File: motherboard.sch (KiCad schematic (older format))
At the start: 90 parts, among them P1 CONN_02X08, U1 STM32F411-LQFP64, U10 74LS125, U11 74LS125, U12 74LS125, U13 74LS125, U14 PCA9517A, U15 PCA9517A, U16 74LS125, U17 74LS125, U2 STM32F411-LQFP64, U3 AP7313, U4 74LS00, U5 74LS125, U6 FM25V20A-G, U7 FM25V20A-G, U8 FM25V20A-G, U9 FM25V20A-G, Y1 32k, Y2 8M(16pF), Y3 32k, Y4 8M(16pF)

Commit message: Implemented recommendations from design meeting.
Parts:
- added C27, C28: 1uF, symbol C
- added C29, C30, C31, C32, C33: 0.1uF, symbol C
- added R18, R25, R26, R27, R28, R29: 100K, symbol R
- added unit 3 of U4
- added unit 4 of U4
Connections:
- net +3V3: now also C29.1, C31.1, C32.1, R18.2, R25.2, R26.2, R27.2, U4.14 (VCC), U4.14 (VCC)
- net GND: now also C27.1, C28.1, C29.2, C30.2, C31.2, C32.2, C33.2, R28.1, R29.1, U4.7 (GND), U4.7 (GND)
- net GPIO0: now also H1.51 (P51); no longer H1.1 (P1)
- net GPIO1: now also H1.52 (P52); no longer H1.2 (P2)
- net GPIO10: now also H1.39 (P39); no longer H1.13 (P13)
- net GPIO11: now also H1.40 (P40); no longer H1.14 (P14)
- net GPIO12: now also H1.37 (P37); no longer H1.15 (P15)
- net GPIO13: now also U2.2 (PC13); no longer H1.16 (P16), U1.54 (PD2)
- net GPIO2: now also H1.49 (P49); no longer H1.3 (P3)
- net GPIO3: now also H1.50 (P50); no longer H1.4 (P4)
- net GPIO4: now also H1.45 (P45); no longer H1.7 (P7)
- net GPIO5: now also H1.46 (P46); no longer H1.8 (P8)
- net GPIO6: now also H1.43 (P43); no longer H1.9 (P9)
- net GPIO7: now also H1.44 (P44); no longer H1.10 (P10)
- net GPIO8: now also H1.41 (P41); no longer H1.11 (P11)
- net GPIO9: now also H1.42 (P42); no longer H1.12 (P12)
- net I2C2_SCL: now also H1.1 (P1), H1.34 (P34); no longer H1.20 (P20), H1.51 (P51)
- net I2C2_SDA: now also H1.3 (P3), H1.33 (P33); no longer H1.19 (P19), H1.49 (P49)
- net NBUFEN_PRI: now also H1.5 (P5), C30.1; no longer H1.47 (P47)
- net NBUFEN_SEC: now also H1.6 (P6), C33.1; no longer H1.48 (P48)
- net NRST_P: now also C27.2, U4.8; no longer U2.50 (PA15)
- net NRST_S: now also C28.2, U4.11; no longer U1.50 (PA15)
- net RADIO_RR: now also H1.48 (P48); no longer H1.6 (P6)
- net RADIO_RX: now also H1.35 (P35); no longer H1.17 (P17)
- net RADIO_TR: now also H1.47 (P47); no longer H1.5 (P5)
- net RADIO_TX: now also H1.36 (P36), R29.2; no longer H1.18 (P18)
- net SGPIO10: now also H1.18 (P18); no longer H1.36 (P36)
- net SGPIO11: now also H1.15 (P15); no longer H1.37 (P37)
- net SGPIO12: now also H1.16 (P16); no longer H1.38 (P38)
- net SGPIO13: now also H1.13 (P13); no longer H1.39 (P39), U2.2 (PC13)
- net SGPIO5: now also H1.4 (P4); no longer H1.50 (P50)
- net SGPIO6: now also H1.2 (P2); no longer H1.52 (P52)
- net SGPIO7: now also H1.19 (P19); no longer H1.33 (P33)
- net SGPIO8: now also H1.20 (P20); no longer H1.34 (P34)
- net SGPIO9: now also H1.17 (P17); no longer H1.35 (P35)
- net SYS_RESET: now also H1.23 (P23), R28.2; no longer H1.29 (P29)
- net SYS_SCL: now also H1.9 (P9); no longer H1.43 (P43)
- net SYS_SDA: now also H1.11 (P11); no longer H1.41 (P41)
- net SYS_SPI_MISO: now also H1.32 (P32); no longer H1.22 (P22)
- net SYS_SPI_MOSI: now also H1.29 (P29); no longer H1.23 (P23)
- net SYS_SPI_NSS: now also H1.30 (P30); no longer H1.24 (P24)
- net SYS_SPI_SCK: now also H1.31 (P31); no longer H1.21 (P21)
- net SGPIO14 renamed NRST2_P
- net NRST2_P: now also R25.1, U4.10; no longer H1.40 (P40)
- new net NRST1_P: R18.1, U2.50 (PA15), U4.9
- new net NRST1_S: R26.1, U1.50 (PA15), U4.12
- new net NRST2_S: R27.1, U1.54 (PD2), U4.13
- no-connect marks 38 -> 40
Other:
- note added: "Not Populated - Tie Down if Unused"
- moved on the sheet: R1, R2, R3, R4, R5, R6, R7, R8, R9, TP1, TP2, TP3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

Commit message: Began placing new components
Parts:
- C27, C28, C29, C30, C31, C32, C33: footprint (none) -> Capacitors_SMD:C_0805_HandSoldering
- R18, R25, R26, R27, R28, R29: footprint (none) -> Resistors_SMD:R_0805_HandSoldering

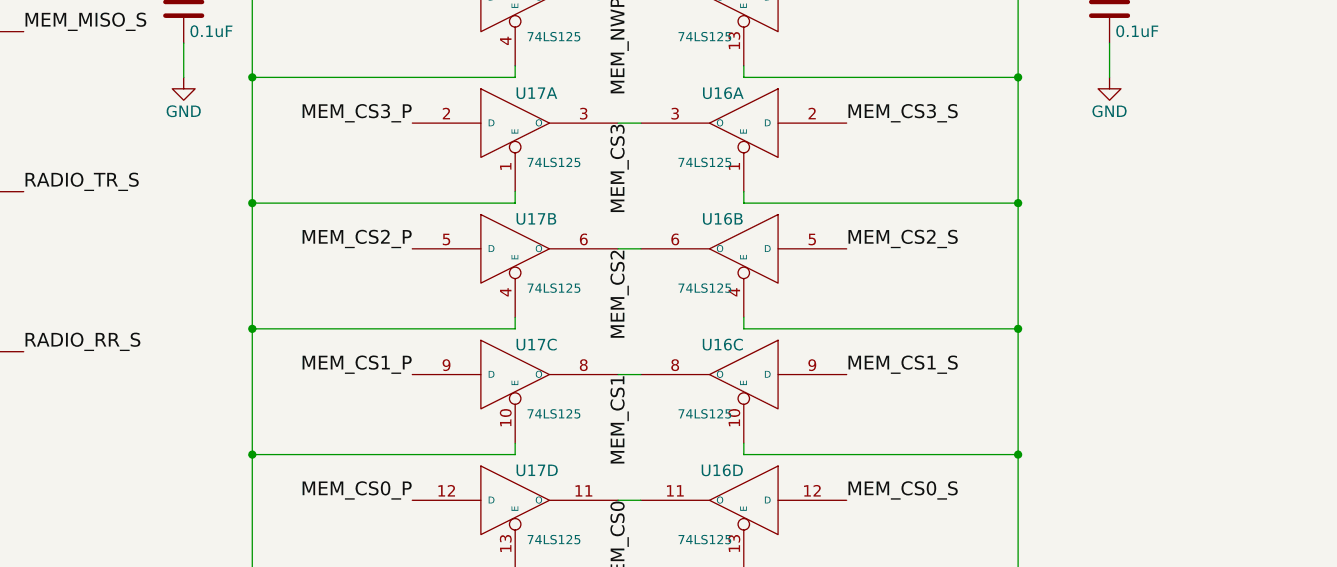
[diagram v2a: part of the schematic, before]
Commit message: All components placed
Most signals routed
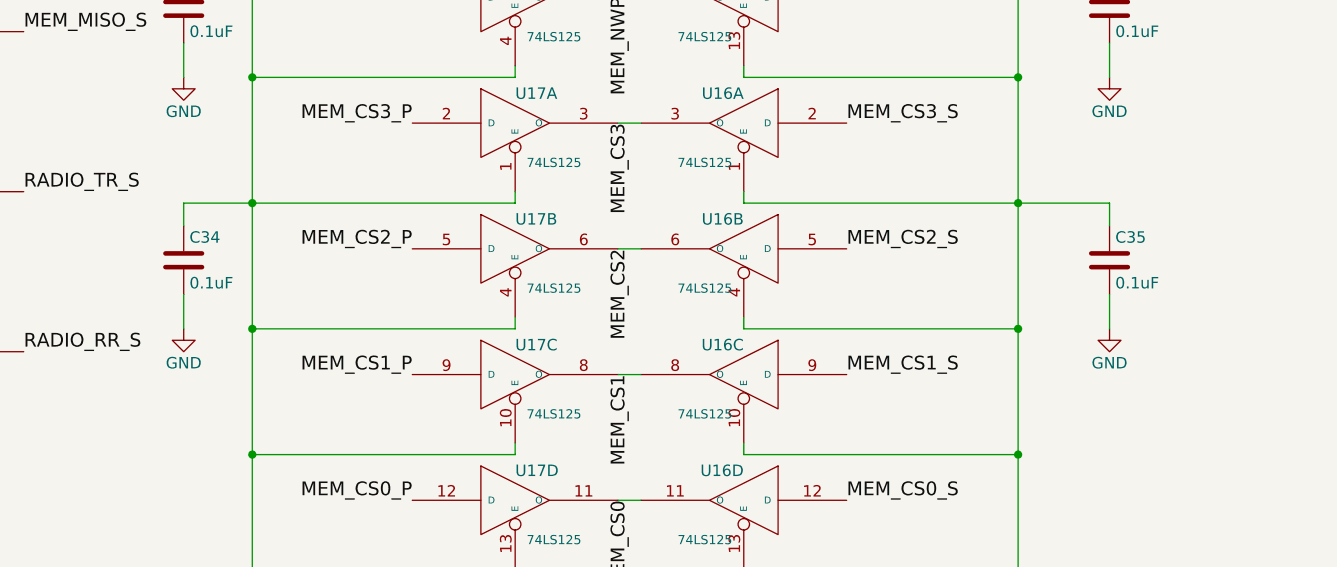
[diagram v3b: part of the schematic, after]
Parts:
- added C34, C35: 0.1uF, Capacitors_SMD:C_0805_HandSoldering, symbol C
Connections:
- net GND: now also C34.2, C35.2
- net NBUFEN_PRI: now also C34.1
- net NBUFEN_SEC: now also C35.1
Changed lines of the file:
@@
 	8350 1950 8350 2150
 Wire Wire Line
-	14150 2400 12950 2400
+	12950 2400 14550 2400
 Wire Wire Line
 	12950 2400 12950 2350
@@
 	11950 2950 11950 2900
 Wire Wire Line
-	11950 2350 11950 2400
+	11950 2400 11950 2350
 Wire Wire Line
 	12400 3150 12500 3150
@@
 Connection ~ 10800 3500
 Wire Wire Line
-	11950 2400 10800 2400
+	10500 2400 11950 2400
 Connection ~ 10800 2950
 Wire Wire Line
@@
 Text Notes 13950 8650 0    60   ~ 0
 Not Populated - Tie Down if Unused
+$Comp
+L GND #PWR062
+U 1 1 5900142E
+P 10500 2950
+F 0 "#PWR062" H 10500 2700 50  0001 C CNN
+F 1 "GND" H 10500 2800 50  0000 C CNN
+F 2 "" H 10500 2950 50  0000 C CNN
+F 3 "" H 10500 2950 50  0000 C CNN
+	1    10500 2950
+	1    0    0    -1
+$EndComp
+$Comp
+L C C34
+U 1 1 59001434
+P 10500 2650
+F 0 "C34" H 10525 2750 50  0000 L CNN
+F 1 "0.1uF" H 10525 2550 50  0000 L CNN
+F 2 "Capacitors_SMD:C_0805_HandSoldering" H 10538 2500 50  0001 C CNN
+F 3 "" H 10500 2650 50  0000 C CNN
+	1    10500 2650
+	1    0    0    -1
+$EndComp
+Wire Wire Line
+	10500 2950 10500 2800
+Wire Wire Line
+	10500 2400 10500 2500
+$Comp
+L GND #PWR063
+U 1 1 5900389F
+P 14550 2950
+F 0 "#PWR063" H 14550 2700 50  0001 C CNN
+F 1 "GND" H 14550 2800 50  0000 C CNN
+F 2 "" H 14550 2950 50  0000 C CNN
+F 3 "" H 14550 2950 50  0000 C CNN
+	1    14550 2950
+	1    0    0    -1
+$EndComp
+$Comp
+L C C35
+U 1 1 590038A5
+P 14550 2650
+F 0 "C35" H 14575 2750 50  0000 L CNN
+F 1 "0.1uF" H 14575 2550 50  0000 L CNN
+F 2 "Capacitors_SMD:C_0805_HandSoldering" H 14588 2500 50  0001 C CNN
+F 3 "" H 14550 2650 50  0000 C CNN
+	1    14550 2650
+	1    0    0    -1
+$EndComp
+Wire Wire Line
+	14550 2950 14550 2800
+Wire Wire Line
+	14550 2400 14550 2500
 $EndSCHEMATC

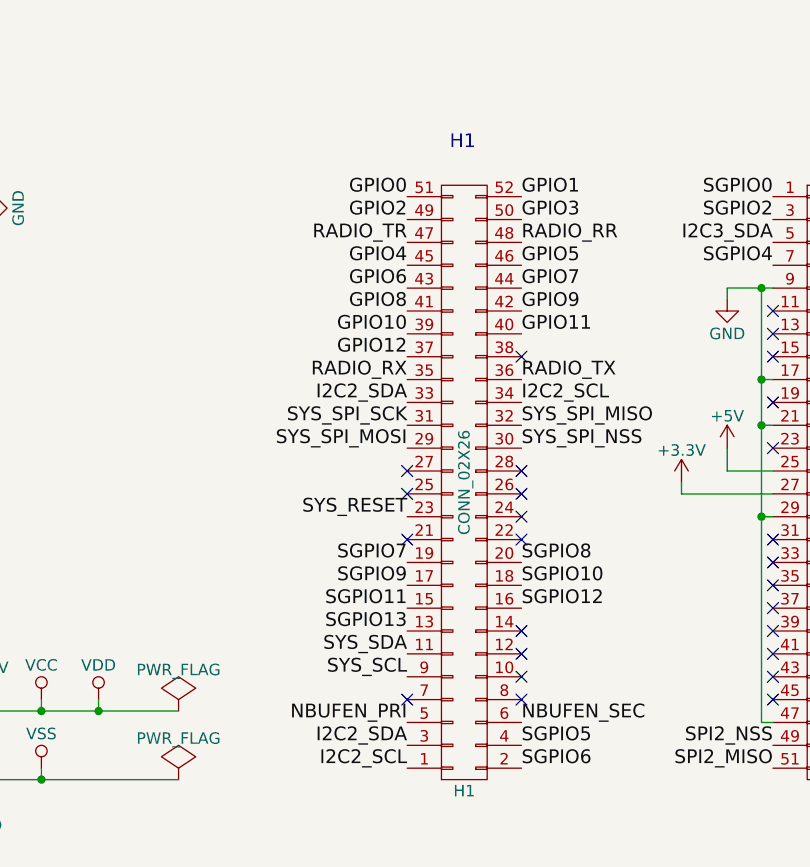
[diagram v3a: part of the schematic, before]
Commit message: Replaced backwards CSK headers
Connectors were mirrored, so that sucks. Connectors replaced,
but all traces to headers need to be re-routed.
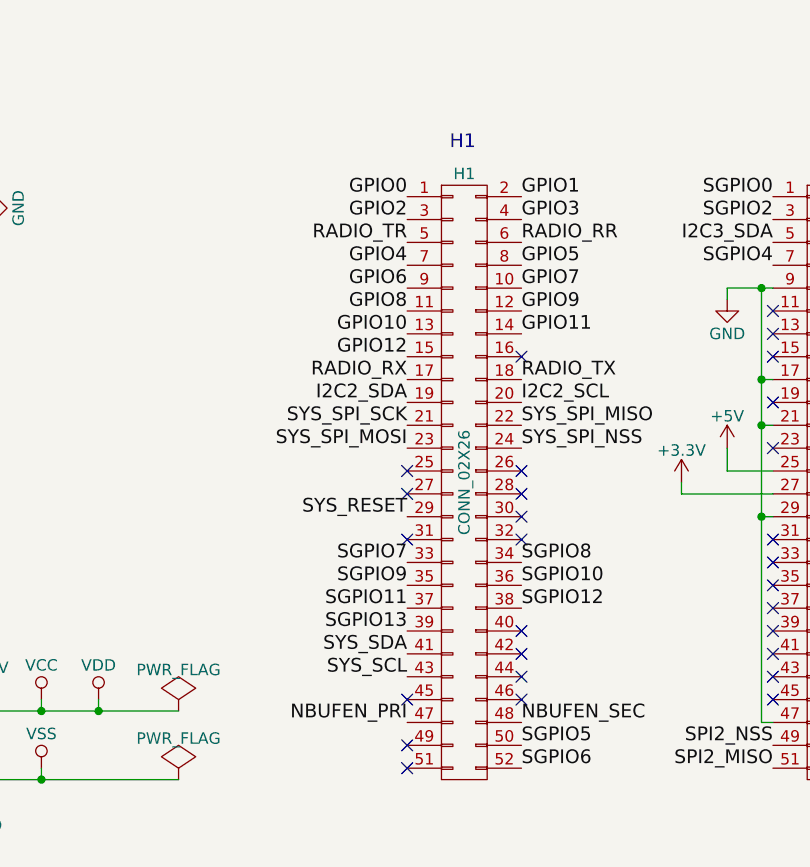
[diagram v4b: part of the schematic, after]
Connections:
- net GPIO0: now also H1.1 (P1); no longer H1.51 (P51)
- net GPIO1: now also H1.2 (P2); no longer H1.52 (P52)
- net GPIO10: now also H1.13 (P13); no longer H1.39 (P39)
- net GPIO11: now also H1.14 (P14); no longer H1.40 (P40)
- net GPIO12: now also H1.15 (P15); no longer H1.37 (P37)
- net GPIO2: now also H1.3 (P3); no longer H1.49 (P49)
- net GPIO3: now also H1.4 (P4); no longer H1.50 (P50)
- net GPIO4: now also H1.7 (P7); no longer H1.45 (P45)
- net GPIO5: now also H1.8 (P8); no longer H1.46 (P46)
- net GPIO6: now also H1.9 (P9); no longer H1.43 (P43)
- net GPIO7: now also H1.10 (P10); no longer H1.44 (P44)
- net GPIO8: now also H1.11 (P11); no longer H1.41 (P41)
- net GPIO9: now also H1.12 (P12); no longer H1.42 (P42)
- net I2C2_SCL: now also H1.20 (P20); no longer H1.1 (P1), H1.34 (P34)
- net I2C2_SDA: now also H1.19 (P19); no longer H1.3 (P3), H1.33 (P33)
- net NBUFEN_PRI: now also H1.47 (P47); no longer H1.5 (P5)
- net NBUFEN_SEC: now also H1.48 (P48); no longer H1.6 (P6)
- net RADIO_RR: now also H1.6 (P6); no longer H1.48 (P48)
- net RADIO_RX: now also H1.17 (P17); no longer H1.35 (P35)
- net RADIO_TR: now also H1.5 (P5); no longer H1.47 (P47)
- net RADIO_TX: now also H1.18 (P18); no longer H1.36 (P36)
- net SGPIO10: now also H1.36 (P36); no longer H1.18 (P18)
- net SGPIO11: now also H1.37 (P37); no longer H1.15 (P15)
- net SGPIO12: now also H1.38 (P38); no longer H1.16 (P16)
- net SGPIO13: now also H1.39 (P39); no longer H1.13 (P13)
- net SGPIO5: now also H1.50 (P50); no longer H1.4 (P4)
- net SGPIO6: now also H1.52 (P52); no longer H1.2 (P2)
- net SGPIO7: now also H1.33 (P33); no longer H1.19 (P19)
- net SGPIO8: now also H1.34 (P34); no longer H1.20 (P20)
- net SGPIO9: now also H1.35 (P35); no longer H1.17 (P17)
- net SYS_RESET: now also H1.29 (P29); no longer H1.23 (P23)
- net SYS_SCL: now also H1.43 (P43); no longer H1.9 (P9)
- net SYS_SDA: now also H1.41 (P41); no longer H1.11 (P11)
- net SYS_SPI_MISO: now also H1.22 (P22); no longer H1.32 (P32)
- net SYS_SPI_MOSI: now also H1.23 (P23); no longer H1.29 (P29)
- net SYS_SPI_NSS: now also H1.24 (P24); no longer H1.30 (P30)
- net SYS_SPI_SCK: now also H1.21 (P21); no longer H1.31 (P31)
- no-connect marks 40 -> 42
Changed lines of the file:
@@
 F 3 "" H 9150 8900 50  0000 C CNN
 	1    9150 9600
-	1    0    0    1
+	1    0    0    -1
 $EndComp
 Text Notes 10800 8150 2    60   ~ 0
@@
 Text Label 8900 10650 2    60   ~ 0
 NBUFEN_PRI
-Text Label 8900 10750 2    60   ~ 0
-I2C2_SDA
-Text Label 8900 10850 2    60   ~ 0
-I2C2_SCL
 Text Label 9400 10850 0    60   ~ 0
 SGPIO6
@@
 Wire Wire Line
 	14550 2400 14550 2500
+NoConn ~ 8900 10750
+NoConn ~ 8900 10850
 $EndSCHEMATC

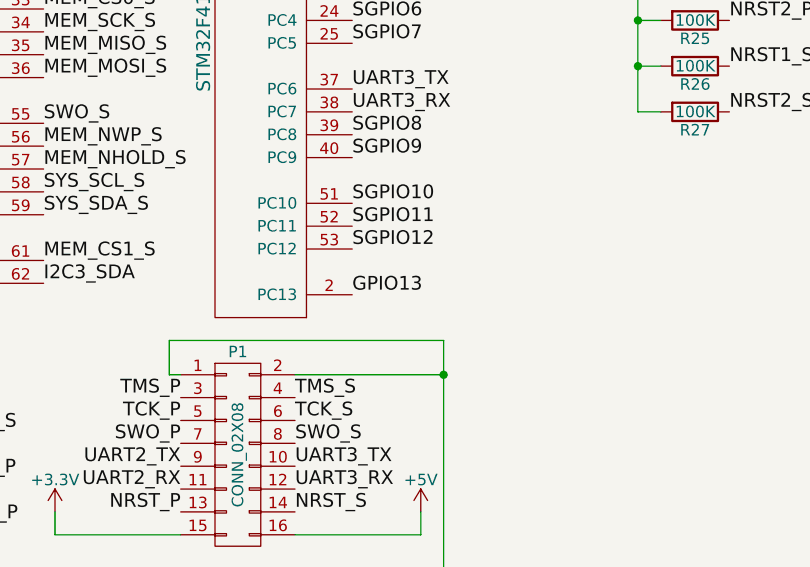
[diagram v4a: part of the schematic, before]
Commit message: Primary GPIO routed
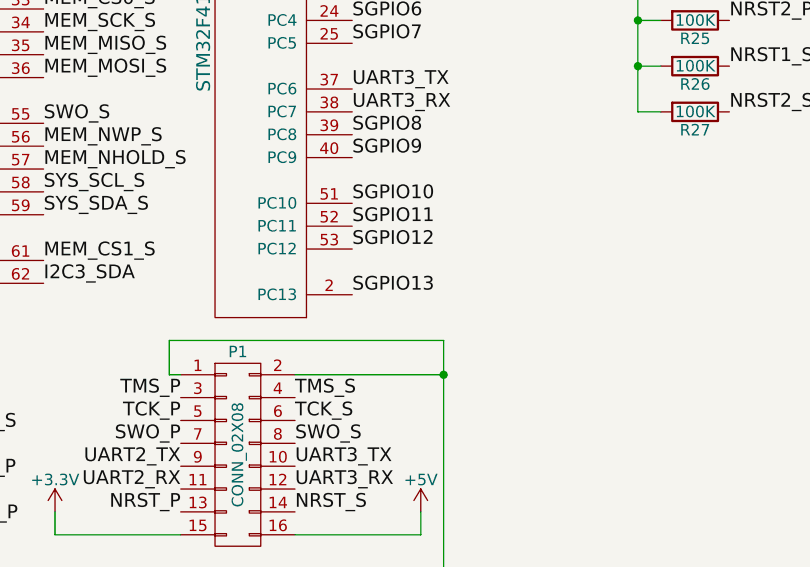
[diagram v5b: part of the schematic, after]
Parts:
- H1, H2: footprint Socket_Strips:Socket_Strip_Straight_2x26 -> motherboard:CSK_Header
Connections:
- net GPIO13 is gone; now on net SGPIO13: U2.2 (PC13)
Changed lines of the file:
@@
 F 0 "H1" H 9150 10950 50  0000 C CNN
 F 1 "CONN_02X26" V 9150 9600 50  0000 C CNN
-F 2 "Socket_Strips:Socket_Strip_Straight_2x26" H 9150 8900 50  0001 C CNN
+F 2 "motherboard:CSK_Header" H 9150 8900 50  0001 C CNN
 F 3 "" H 9150 8900 50  0000 C CNN
 	1    9150 9600
@@
 F 0 "H2" H 10750 10950 50  0000 C CNN
 F 1 "CONN_02X26" V 10750 9600 50  0000 C CNN
-F 2 "Socket_Strips:Socket_Strip_Straight_2x26" H 10750 8900 50  0001 C CNN
+F 2 "motherboard:CSK_Header" H 10750 8900 50  0001 C CNN
 F 3 "" H 10750 8900 50  0000 C CNN
 	1    10750 9600
@@
 GPIO12
 Text Label 4150 4800 0    60   ~ 0
-GPIO13
+SGPIO13
 Text Label 1450 2550 0    60   ~ 0
 NRST1_S

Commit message: Added footprint directory
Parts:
- U6, U7, U8, U9: footprint Housings_SOIC:SOIC-8_3.9x4.9mm_Pitch1.27mm -> FM25V20A-G:SOIC127P800X203-8N
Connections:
- net +3V3: no longer R18.2, R25.2, R26.2, R27.2
- net GND: now also R18.2, R25.2, R26.2, R27.2; no longer C33.2, C35.2
- net NBUFEN_SEC: no longer C33.1, C35.1
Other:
- moved on the sheet: C23, C24, C25, C26, C30, C31, C32, C33, C34, C35, R10, R11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
